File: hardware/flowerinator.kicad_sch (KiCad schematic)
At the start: 9 parts, among them M1 Motor_DC, Q1 Q_NMOS_GDS, Q2 Q_NMOS_GDS, U1 ESP32-WROOM-32, U2 Water sensor, U3 Soil Sensor, U4 Height Sensor

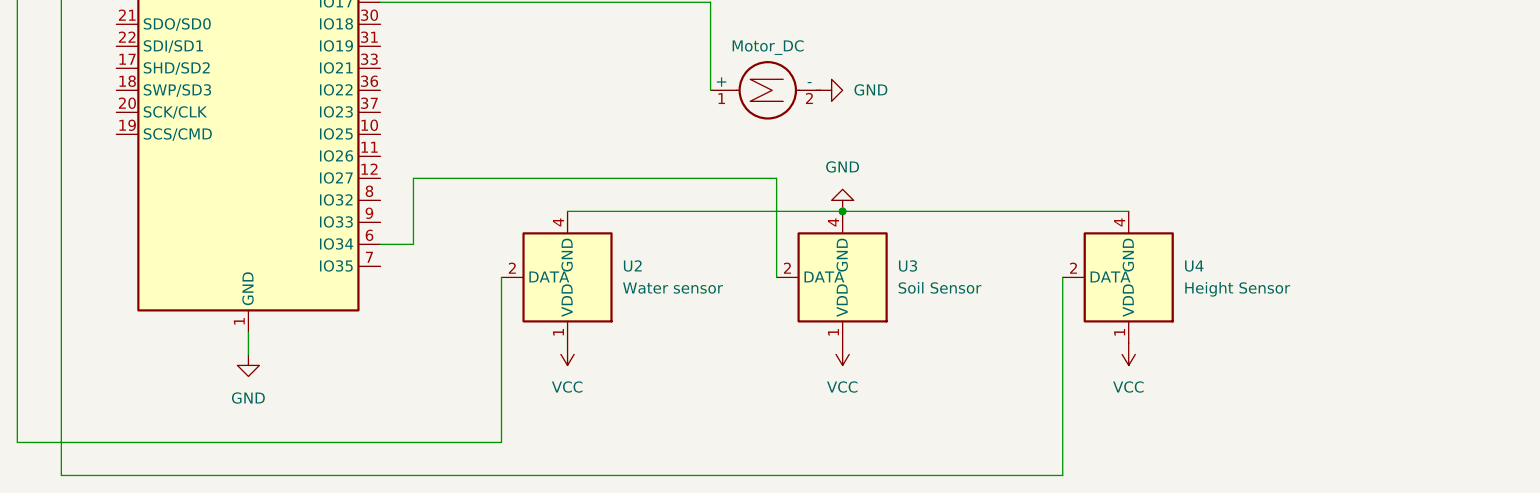
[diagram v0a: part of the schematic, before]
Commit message: added second humidity sensor
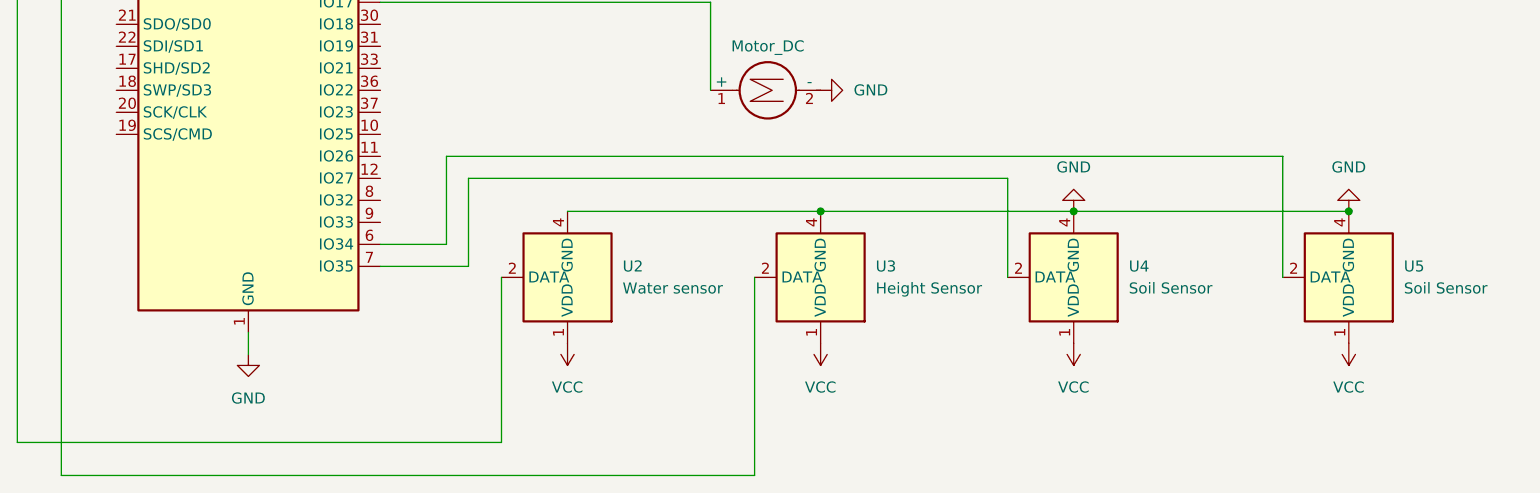
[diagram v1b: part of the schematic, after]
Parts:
- added U5: Soil Sensor, Sensor:Aosong_DHT11_5.5x12.0_P2.54mm, symbol Sensor:CHT11
- renumbered U4 to U3, U3 to U4
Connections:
- net GND: now also U5.4 (GND)
- net VCC: now also U5.1 (VDD)
- net at U1.6 (IO34): now also U5.2 (DATA); no longer U4.2 (DATA)
- net at U1.7 (IO35): now also U4.2 (DATA)
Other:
- moved on the sheet: U3, U4

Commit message: almost finished the arduino code
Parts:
- added J1: HY-SRF05 ultrasonic, symbol Connector:Conn_01x05_Pin
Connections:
- net GND: now also J1.4 (GND)
- net at U1.36 (IO22): now also J1.3 (Echo)
- net at U1.37 (IO23): now also J1.2 (Trigger)
- new net +5V: J1.1 (Vcc)
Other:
- moved on the sheet: Q2

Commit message: finished the pcb
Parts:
- removed Q1, Q2: Q_NMOS_GDS, symbol Transistor_FET:Q_NMOS_GDS
- removed U1: ESP32-WROOM-32, RF_Module:ESP32-WROOM-32, symbol RF_Module:ESP32-WROOM-32
- added J10, J5, J6, J7, J8: Screw_Terminal_01x03, Connector_Phoenix_GMSTB:PhoenixContact_GMSTBVA_2,5_3-G_1x03_P7.50mm_Vertical, symbol Connector:Screw_Terminal_01x03
- added J2, J4: Screw_Terminal_01x02, Connector_Phoenix_GMSTB:PhoenixContact_GMSTBVA_2,5_2-G_1x02_P7.50mm_Vertical, symbol Connector:Screw_Terminal_01x02
- added J3: Screw_Terminal_01x02, Connector_Phoenix_GMSTB:PhoenixContact_GMSTBV_2,5_2-GF-7,62_1x02_P7.62mm_Vertical_ThreadedFlange, symbol Connector:Screw_Terminal_01x02
- added J9: Screw_Terminal_01x05, Connector_Phoenix_GMSTB:PhoenixContact_GMSTBVA_2,5_5-G_1x05_P7.50mm_Vertical, symbol Connector:Screw_Terminal_01x05
- added Q2, Q3, Q4: FDMS8350LET40, Package_TO_SOT_SMD:TDSON-8-1, symbol Transistor_FET:FDMS8350LET40
- added U6: ESP32-C3-DevKitM-1, RF_Module:ESP32-C3-DevKitM-1, symbol RF_Module:ESP32-C3-DevKitM-1
- U3: value Height Sensor -> Touch Sensor
- U5: value Soil Sensor -> Soil Sensor2
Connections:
- net +5V: no longer J1.1 (Vcc)
- net GND: no longer J1.4 (GND), L1. (-), M1.2 (-), U2.4 (GND), U3.4 (GND), U4.4 (GND), U5.4 (GND), W1. (-)
- removed net VCC: U2.1 (VDD), U3.1 (VDD), U4.1 (VDD), U5.1 (VDD)
- new net: J10.2 (Pin_2), J5.3 (Pin_3), J6.3 (Pin_3), J7.3 (Pin_3), J8.3 (Pin_3), J9.4 (Pin_4), Q2.1 (S), Q2.2 (S), Q2.3 (S), Q3.1 (S), Q3.2 (S), Q3.3 (S), Q4.1 (S), Q4.2 (S), Q4.3 (S), U6.1 (GND), U6.12 (GND), U6.15 (GND), U6.16 (GND), U6.19 (GND), U6.24 (GND), U6.27 (GND), U6.30 (GND), U6.6 (GND), U6.8 (GND)
- new net: Q2.4 (G), U6.17 (IO19)
- new net: J2.2 (Pin_2), Q2.5 (D)
- new net: Q4.4 (G), U6.23 (IO7)
- new net: J4.2 (Pin_2), Q4.5 (D)
- new net: J10.1 (Pin_1), J2.1 (Pin_1), J3.1 (Pin_1), J4.1 (Pin_1), J5.1 (Pin_1), J6.1 (Pin_1), J7.1 (Pin_1), J8.1 (Pin_1), J9.1 (Pin_1), U6.13 (5V), U6.14 (5V)
- new net: J10.3 (Pin_3), U6.2 (3V3), U6.3 (3V3)
- new net: J8.2 (Pin_2), U6.22 (IO6)
- new net: Q3.4 (G), U6.18 (IO18)
- new net: J3.2 (Pin_2), Q3.5 (D)
- new net: J6.2 (Pin_2), U6.20 (IO4)
- new net: J9.2 (Pin_2), U6.10 (IO1)
- new net: J9.3 (Pin_3), U6.4 (IO2)
- new net: J7.2 (Pin_2), U6.21 (IO5)
- new net: J5.2 (Pin_2), U6.5 (IO3)
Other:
- note added: "J2 -- Pump J3 -- Led J4 -- Motor"
- note added: "J9 -- US sensor J5 -- Soil sensor 1 J6 -- Soild sensor 2 J7 -- Water sensor J8 -- Touch sensor"
- moved on the sheet: J1, U2, U3, U4, U5

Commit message: schematic
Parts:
- J3: footprint Connector_Phoenix_GMSTB:PhoenixContact_GMSTBV_2,5_2-GF-7,62_1x02_P7.62mm_Vertical_ThreadedFlange -> Connector_Phoenix_GMSTB:PhoenixContact_GMSTBVA_2,5_2-G_1x02_P7.50mm_Vertical
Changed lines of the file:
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@@
 			)
 		)
-		(property "Footprint" "Connector_Phoenix_GMSTB:PhoenixContact_GMSTBV_2,5_2-GF-7,62_1x02_P7.62mm_Vertical_ThreadedFlange"
+		(property "Footprint" "Connector_Phoenix_GMSTB:PhoenixContact_GMSTBVA_2,5_2-G_1x02_P7.50mm_Vertical"
 			(at 41.91 129.54 0)
 			(hide yes)

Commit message: documentation
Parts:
- L1: footprint (none) -> -
- M1: footprint (none) -> 12GA-N20 Miniature DC Metal Gear Motor 3V 3.7V 5V 6V 12V Low RPM High Torque 4WD Car Electric Screwdriver Door Lock Mot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
- U2, U3: footprint Sensor:Aosong_DHT11_5.5x12.0_P2.54mm -> -
- U4, U5: footprint Sensor:Aosong_DHT11_5.5x12.0_P2.54mm -> Capacitive Soil Moisture Sensor Module Corrosion Resistant 3.3~5.5V for Arduino Moisture Detection
- W1: footprint (none) -> DC 3V 5V Micro Submersible Mini Water Pump for Aquariums Fish Tank Fountain Hydroponics
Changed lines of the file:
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@@
 			)
 		)
-		(property "Footprint" "Sensor:Aosong_DHT11_5.5x12.0_P2.54mm"
+		(property "Footprint" "-"
 			(at 205.74 148.59 0)
 			(hide yes)
@@
 			)
 		)
-		(property "Datasheet" "http://aosong.com/en/products-21.html"
+		(property "Datasheet" "https://www.aliexpress.com/item/1005007439447804.html"
 			(at 201.93 132.08 0)
 			(hide yes)
@@
 			)
 		)
-		(property "Description" "Temperature and humidity module"
+		(property "Description" "Horizontal Float Sensor Switch Side Mount Liquid Water Level Sensor Controller Automatic Water Pump Controller"
 			(at 205.74 138.43 0)
 			(hide yes)
@@
 			)
 		)
-		(property "Footprint" ""
+		(property "Footprint" "DC 3V 5V Micro Submersible Mini Water Pump for Aquariums Fish Tank Fountain Hydroponics"
 			(at 231.14 52.07 0)
 			(hide yes)
@@
 			)
 		)
-		(property "Datasheet" "https://www.instructables.com/Arduino-Soil-Moisture-Sensor/"
+		(property "Datasheet" "https://www.aliexpress.com/item/1005004451967987.html"
 			(at 231.14 52.07 0)
 			(hide yes)
@@
 			)
 		)
-		(property "Footprint" "Sensor:Aosong_DHT11_5.5x12.0_P2.54mm"
+		(property "Footprint" "-"
 			(at 205.74 166.37 0)
 			(hide yes)
@@
 			)
 		)
-		(property "Datasheet" "http://aosong.com/en/products-21.html"
+		(property "Datasheet" "https://www.aliexpress.com/item/1005009348155914.html"
 			(at 201.93 149.86 0)
 			(hide yes)
@@
 			)
 		)
-		(property "Description" "Temperature and humidity module"
+		(property "Description" "TTP223B Digital Touch Blue Digital Sensor Module Capacitive Touch Switch for Arduino"
 			(at 205.74 156.21 0)
 			(hide yes)
@@
 			)
 		)
-		(property "Datasheet" ""
+		(property "Datasheet" "https://www.aliexpress.com/item/1005004679967893.html"
 			(at 97.79 60.96 0)
 			(hide yes)
@@
 			)
 		)
-		(property "Datasheet" ""
+		(property "Datasheet" "https://www.aliexpress.com/item/1005004679967893.html"
 			(at 134.62 139.7 0)
 			(hide yes)
@@
 			)
 		)
-		(property "Footprint" "Sensor:Aosong_DHT11_5.5x12.0_P2.54mm"
+		(property "Footprint" "Capacitive Soil Moisture Sensor Module Corrosion Resistant 3.3~5.5V for Arduino Moisture Detection"
 			(at 205.74 129.54 0)
 			(hide yes)
@@
 			)
 		)
-		(property "Datasheet" "http://aosong.com/en/products-21.html"
+		(property "Datasheet" "https://www.aliexpress.com/item/1005008744986367.html"
 			(at 201.93 113.03 0)
 			(hide yes)
@@
 	(symbol
 		(lib_id "lib:Led_strip")
-		(at 234.95 36.83 0)
+		(at 231.14 38.1 0)
 		(unit 1)
 		(body_style 1)
@@
 		(dnp no)
 		(property "Reference" "L1"
-			(at 237.236 29.972 0)
+			(at 233.426 31.242 0)
 			(hide yes)
 			(show_name no)
@@
 		)
 		(property "Value" "Led Strip"
-			(at 238.76 40.894 0)
-			(show_name no)
-			(do_not_autoplace no)
-			(effects
-				(font
-					(size 1.27 1.27)
-				)
-			)
-		)
-		(property "Footprint" ""
-			(at 234.95 36.83 0)
-			(hide yes)
-			(show_name no)
-			(do_not_autoplace no)
-			(effects
-				(font
-					(size 1.27 1.27)
-				)
-			)
-		)
-		(property "Datasheet" ""
-			(at 234.95 36.83 0)
-			(hide yes)
-			(show_name no)
-			(do_not_autoplace no)
-			(effects
-				(font
-					(size 1.27 1.27)
-				)
-			)
-		)
-		(property "Description" ""
-			(at 234.95 36.83 0)
+			(at 234.95 42.164 0)
+			(show_name no)
+			(do_not_autoplace no)
+			(effects
+				(font
+					(size 1.27 1.27)
+				)
+			)
+		)
+		(property "Footprint" "-"
+			(at 231.14 38.1 0)
+			(hide yes)
+			(show_name no)
+			(do_not_autoplace no)
+			(effects
+				(font
+					(size 1.27 1.27)
+				)
+			)
+		)
+		(property "Datasheet" "https://www.aliexpress.com/item/1005007486917090.html"
+			(at 231.14 38.1 0)
+			(hide yes)
+			(show_name no)
+			(do_not_autoplace no)
+			(effects
+				(font
+					(size 1.27 1.27)
+				)
+			)
+		)
+		(property "Description" "Growing led lights"
+			(at 231.14 38.1 0)
 			(hide yes)
 			(show_name no)
@@
 			)
 		)
-		(property "Datasheet" ""
+		(property "Datasheet" "https://www.aliexpress.com/item/1005007024869146.html"
 			(at 242.57 147.32 0)
 			(hide yes)
@@
 			)
 		)
-		(property "Datasheet" ""
+		(property "Datasheet" "https://www.aliexpress.com/item/1005004679967893.html"
 			(at 134.62 119.38 0)
 			(hide yes)
@@
 			)
 		)
-		(property "Footprint" ""
+		(property "Footprint" "12GA-N20 Miniature DC Metal Gear Motor 3V 3.7V 5V 6V 12V Low RPM High Torque 4WD Car Electric Screwdriver Door Lock Motor"
 			(at 232.156 63.5 0)
 			(hide yes)
@@
 			)
 		)
-		(property "Datasheet" ""
+		(property "Datasheet" "https://www.aliexpress.com/item/4001195504462.html"
 			(at 232.156 63.5 0)
 			(hide yes)
@@
 			)
 		)
-		(property "Datasheet" ""
+		(property "Datasheet" "https://www.aliexpress.com/item/1005004679967893.html"
 			(at 41.91 129.54 0)
 			(hide yes)
@@
 			)
 		)
-		(property "Datasheet" ""
+		(property "Datasheet" "https://www.aliexpress.com/item/1005004679967893.html"
 			(at 134.62 129.54 0)
 			(hide yes)
@@
 			)
 		)
-		(property "Datasheet" ""
+		(property "Datasheet" "https://www.aliexpress.com/item/1005004679967893.html"
 			(at 41.91 143.51 0)
 			(hide yes)
@@
 			)
 		)
-		(property "Datasheet" ""
+		(property "Datasheet" "https://www.aliexpress.com/item/1005004679967893.html"
 			(at 41.91 116.84 0)
 			(hide yes)
@@
 			)
 		)
-		(property "Datasheet" ""
+		(property "Datasheet" "https://www.aliexpress.com/item/1005004679967893.html"
 			(at 134.62 109.22 0)
 			(hide yes)
@@
 			)
 		)
-		(property "Footprint" "Sensor:Aosong_DHT11_5.5x12.0_P2.54mm"
+		(property "Footprint" "Capacitive Soil Moisture Sensor Module Corrosion Resistant 3.3~5.5V for Arduino Moisture Detection"
 			(at 205.74 110.49 0)
 			(hide yes)
@@
 			)
 		)
-		(property "Datasheet" "http://aosong.com/en/products-21.html"
+		(property "Datasheet" "https://www.aliexpress.com/item/1005008744986367.html"
 			(at 201.93 93.98 0)
 			(hide yes)
